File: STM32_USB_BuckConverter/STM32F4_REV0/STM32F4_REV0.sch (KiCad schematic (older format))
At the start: 41 parts

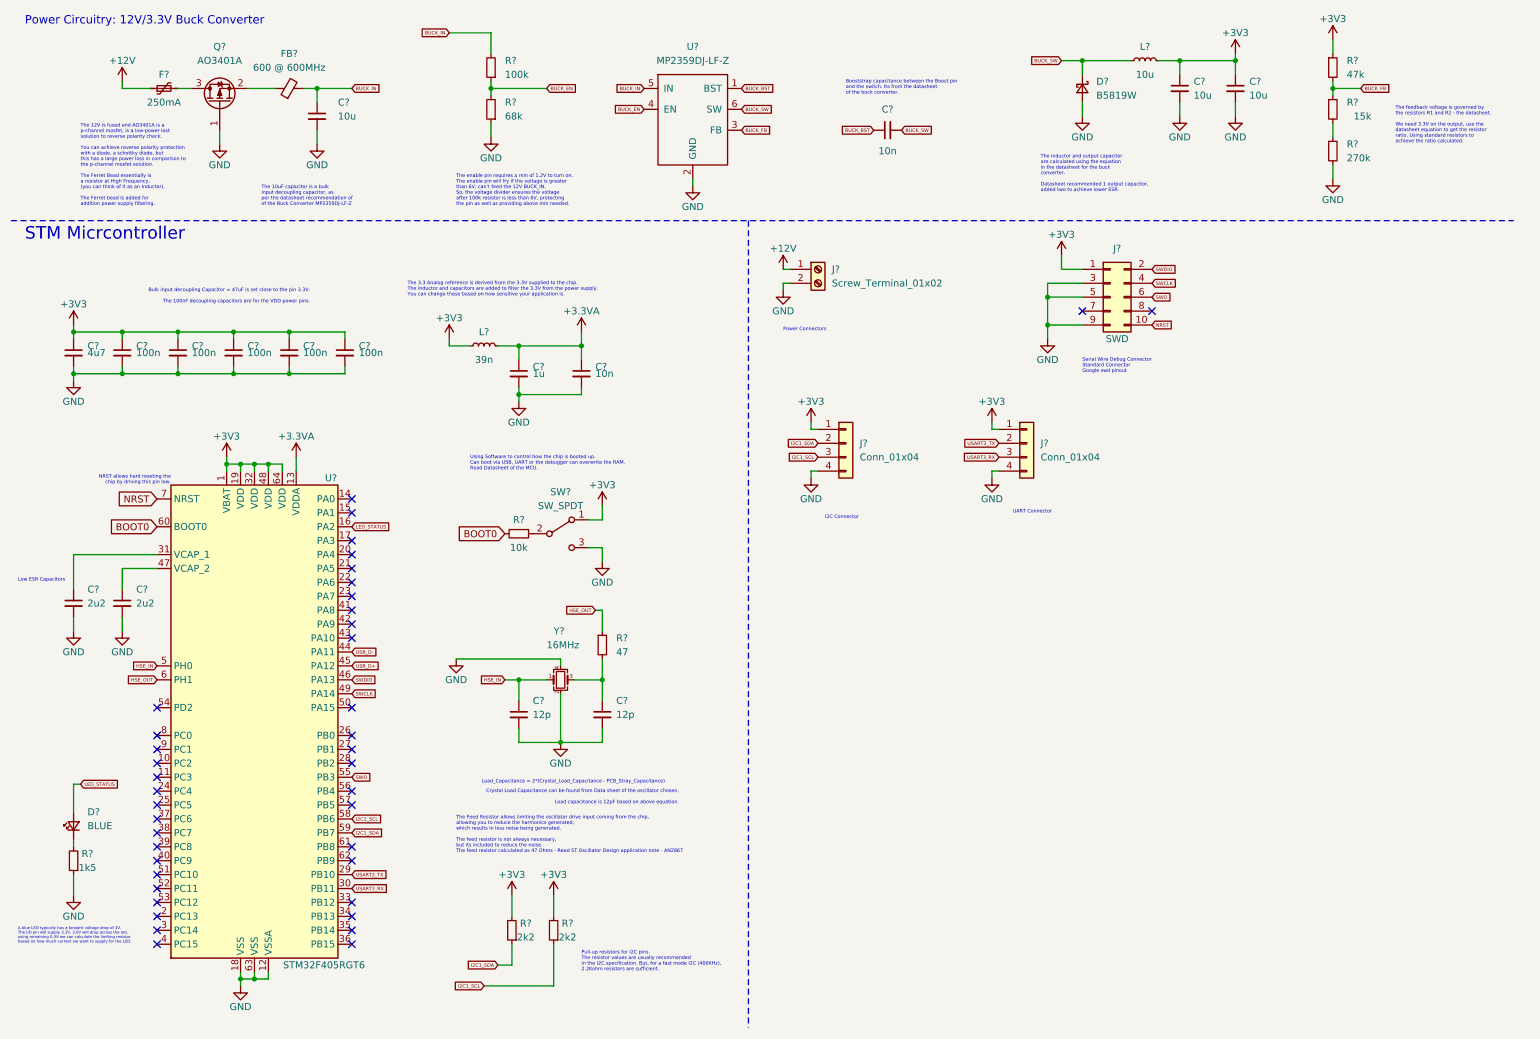
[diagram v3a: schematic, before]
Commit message: Added USB micro connector. Also added schottky diode in the power circuitry incase we want to power the board with USB and not the 12V. The schottky diode will protect incase both 12V present and the USB connected, the 12V will reverse biase the schottky diode.
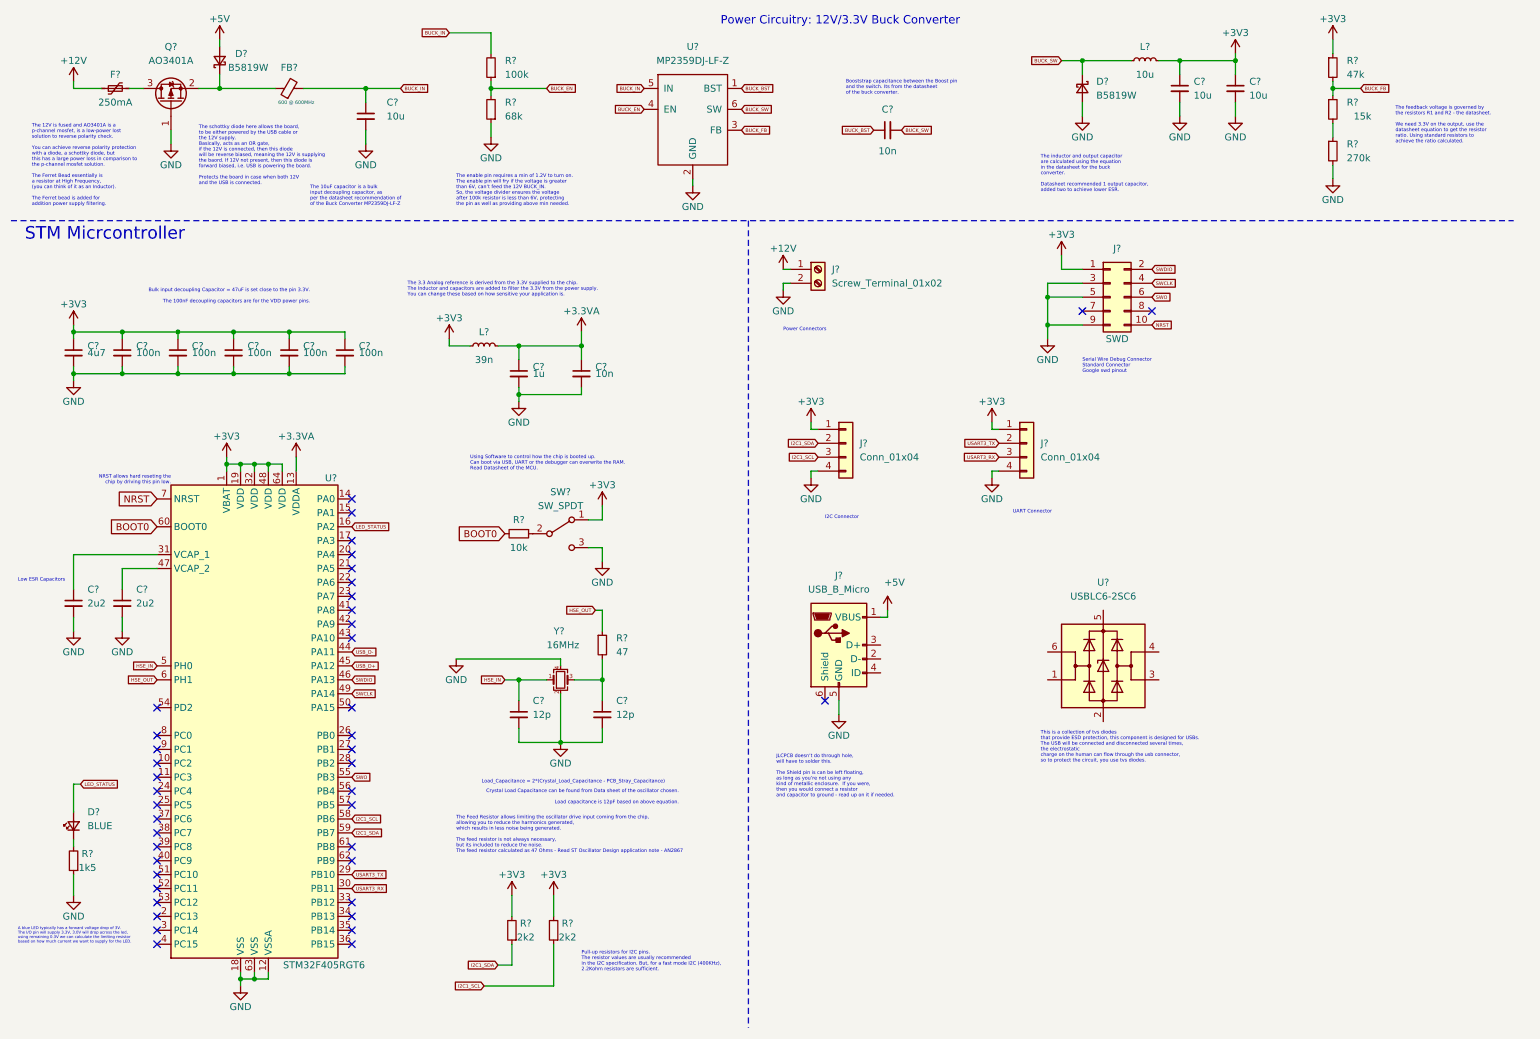
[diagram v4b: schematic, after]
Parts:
- added D?: B5819W, symbol Device:D_Schottky_Small
- added J?: USB_B_Micro, symbol Connector:USB_B_Micro
- added U?: USBLC6-2SC6, Package_TO_SOT_SMD:SOT-23-6, symbol Power_Protection:USBLC6-2SC6
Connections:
- net GND: now also J?.5 (GND)
- net at FB?.1, Q?.2 (S): now also D?.1 (K)
- new net +5V: D?.2 (A), J?.1 (VBUS)
- no-connect marks 41 -> 42
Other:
- note added: "JLCPCB doesn’t do through hole, \nwill have to solder this. \n\nThe Shield pin is can be left floating, \nas long as you’re not using any \nkind of metallic enclosure. If you were, \nthen you would connect a resistor\nand capacitor to ground - read up on it if needed."
- note added: "The schottky diode here allows the board, \nto be either powered by the USB cable or \nthe 12V supply. \nBasically, acts as an OR gate, \nif the 12V is connected, then this diode\nwill be reverse biased, meaning the 12V is supplying\nthe baord. If 12V not present, then this diode is \nforward biased, i.e. USB is powering the board. \n\nProtects the board in case when both 12V \nand the USB is con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"
- note added: "This is a collection of tvs diodes \nthat provide ESD protection, this component is designed for USBs. \nThe USB will be connected and disconnected several times, \nthe electrostatic\ncharge on the human can flow through the usb connector, \nso to protect the circuit, you use tvs diodes. \n"
- moved on the sheet: C?, F?, Q?
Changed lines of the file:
@@
-$EndComp
-$Comp
-L power:+12V #PWR?
-U 1 1 6070A53E
-P 1250 1000
-F 0 "#PWR?" H 1250 850 50  0001 C CNN
-F 1 "+12V" H 1250 1150 50  0000 C CNN
-F 2 "" H 1250 1000 50  0001 C CNN
-F 3 "" H 1250 1000 50  0001 C CNN
-	1    1250 1000
-	1    0    0    -1
-$EndComp
-$Comp
-L Device:Polyfuse_Small F?
-U 1 1 6070BEAF
-P 1550 1050
-F 0 "F?" V 1650 1050 50  0000 C CNN
-F 1 "250mA" V 1450 1050 50  0000 C CNN
-F 2 "" H 1600 850 50  0001 L CNN
-F 3 "~" H 1550 1050 50  0001 C CNN
-	1    1550 1050
-	0    -1   -1   0
-$EndComp
-$Comp
-L power:GND #PWR?
-U 1 1 60714FBD
-P 1950 1450
-F 0 "#PWR?" H 1950 1200 50  0001 C CNN
-F 1 "GND" H 1950 1300 50  0000 C CNN
-F 2 "" H 1950 1450 50  0001 C CNN
-F 3 "" H 1950 1450 50  0001 C CNN
-	1    1950 1450
-	-1   0    0    -1
-$EndComp
-Wire Wire Line
-	1950 1350 1950 1450
-Wire Wire Line
-	1650 1050 1750 1050
-Text Notes 950  1900 0    25   ~ 0
-The 12V is fused and AO3401A is a \np-channel mosfet, is a low-power lost \nsolution to reverse polarity check. \n\nYou can achieve reverse polarity protection \nwith a diode, a schottky diode, but \nthis has a large power loss in comparison to \nthe p-channel mosfet solution. \n\nThe Ferret Bead essentially is \na resistor at High Frequency, \n(you can think of it as an Inductor). \n\nThe Ferret bead is added for \naddition power supply filtering. \n
-Wire Wire Line
-	2350 1050 2150 1050
-$Comp
-L Transistor_FET:AO3401A Q?
-U 1 1 6070E341
-P 1950 1150
-F 0 "Q?" V 2350 1150 50  0000 C CNN
-F 1 "AO3401A" V 2250 1150 50  0000 C CNN
-F 2 "Package_TO_SOT_SMD:SOT-23" H 2150 1075 50  0001 L CIN
-F 3 "http://www.aosmd.com/pdfs/datasheet/AO3401A.pdf" H 1950 1150 50  0001 L CNN
-	1    1950 1150
-	0    -1   -1   0
 $EndComp
 $Comp
@@
 U 1 1 607283EA
 P 2450 1050
-F 0 "FB?" V 2700 1050 50  0000 C CNN
-F 1 "600 @ 600MHz" V 2600 1050 50  0000 C CNN
+F 0 "FB?" V 2600 1050 50  0000 C CNN
+F 1 "600 @ 600MHz" V 2350 1000 25  0000 C CNN
 F 2 "" V 2380 1050 50  0001 C CNN
 F 3 "~" H 2450 1050 50  0001 C CNN
@@
 L Device:C_Small C?
 U 1 1 607304BE
-P 2650 1250
-F 0 "C?" H 2800 1350 50  0000 L CNN
-F 1 "10u" H 2800 1250 50  0000 L CNN
-F 2 "" H 2650 1250 50  0001 C CNN
-F 3 "~" H 2650 1250 50  0001 C CNN
-	1    2650 1250
-	1    0    0    -1
-$EndComp
-Wire Wire Line
-	2550 1050 2650 1050
-Wire Wire Line
-	2650 1050 2650 1150
+P 3000 1250
+F 0 "C?" H 3150 1350 50  0000 L CNN
+F 1 "10u" H 3150 1250 50  0000 L CNN
+F 2 "" H 3000 1250 50  0001 C CNN
+F 3 "~" H 3000 1250 50  0001 C CNN
+	1    3000 1250
+	1    0    0    -1
+$EndComp
+Wire Wire Line
+	3000 1050 3000 1150
 $Comp
 L power:GND #PWR?
 U 1 1 60733C86
-P 2650 1450
-F 0 "#PWR?" H 2650 1200 50  0001 C CNN
-F 1 "GND" H 2650 1300 50  0000 C CNN
-F 2 "" H 2650 1450 50  0001 C CNN
-F 3 "" H 2650 1450 50  0001 C CNN
-	1    2650 1450
-	-1   0    0    -1
-$EndComp
-Wire Wire Line
-	2650 1350 2650 1450
-Text Notes 2250 1900 0    25   ~ 0
+P 3000 1450
+F 0 "#PWR?" H 3000 1200 50  0001 C CNN
+F 1 "GND" H 3000 1300 50  0000 C CNN
+F 2 "" H 3000 1450 50  0001 C CNN
+F 3 "" H 3000 1450 50  0001 C CNN
+	1    3000 1450
+	-1   0    0    -1
+$EndComp
+Wire Wire Line
+	3000 1350 3000 1450
+Text Notes 2600 1900 0    25   ~ 0
 The 10uF capacitor is a bulk \ninput decoupling capacitor, as \nper the datasheet recommendation of \nof the Buck Converter MP2359DJ-LF-Z
-Text GLabel 2900 1050 2    25   Input ~ 0
+Text GLabel 3250 1050 2    25   Input ~ 0
 BUCK_IN
 Wire Wire Line
-	2900 1050 2650 1050
-Connection ~ 2650 1050
+	3250 1050 3000 1050
+Connection ~ 3000 1050
 $Comp
 L Device:R_Small R?
@@
 Wire Notes Line
 	450  2000 11250 2000
-Text Notes 550  600  0    60   ~ 0
+Text Notes 5550 600  0    60   ~ 0
 Power Circuitry: 12V/3.3V Buck Converter
-Wire Wire Line
-	1250 1000 1250 1050
-Wire Wire Line
-	1250 1050 1450 1050
 $Comp
 L Connector:Screw_Terminal_01x02 J?
@@
 Text Notes 7650 4150 0    25   ~ 0
 UART Connector\n\n
+$Comp
+L Connector:USB_B_Micro J?
+U 1 1 608B3BCC
+P 6400 5050
+F 0 "J?" H 6400 5550 50  0000 C CNN
+F 1 "USB_B_Micro" H 6400 5450 50  0000 C CNN
+F 2 "" H 6550 5000 50  0001 C CNN
+F 3 "~" H 6550 5000 50  0001 C CNN
+	1    6400 5050
+	1    0    0    -1
+$EndComp
+$Comp
+L power:GND #PWR?
+U 1 1 608B6CA0
+P 6400 5550
+F 0 "#PWR?" H 6400 5300 50  0001 C CNN
+F 1 "GND" H 6400 5400 50  0000 C CNN
+F 2 "" H 6400 5550 50  0001 C CNN
+F 3 "" H 6400 5550 50  0001 C CNN
+	1    6400 5550
+	-1   0    0    -1
+$EndComp
+Wire Wire Line
+	6400 5550 6400 5450
+NoConn ~ 6300 5450
+Text Notes 5950 6150 0    25   ~ 0
+JLCPCB doesn’t do through hole, \nwill have to solder this. \n\nThe Shield pin is can be left floating, \nas long as you’re not using any \nkind of metallic enclosure.  If you were, \nthen you would connect a resistor\nand capacitor to ground - read up on it if needed.
+$Comp
+L Power_Protection:USBLC6-2SC6 U?
+U 1 1 608C7806
+P 8300 5200
+F 0 "U?" H 8300 5800 50  0000 C CNN
+F 1 "USBLC6-2SC6" H 8300 5700 50  0000 C CNN
+F 2 "Package_TO_SOT_SMD:SOT-23-6" H 8300 4700 50  0001 C CNN
+F 3 "https://www.st.com/resource/en/datasheet/usblc6-2.pdf" H 8500 5550 50  0001 C CNN
+	1    8300 5200
+	1    0    0    -1
+$EndComp
+Text Notes 7850 5900 0    25   ~ 0
+This is a collection of tvs diodes \nthat provide ESD protection, this component is designed for USBs. \nThe USB will be connected and disconnected several times, \nthe electrostatic\ncharge on the human can flow through the usb connector, \nso to protect the circuit, you use tvs diodes. \n
+$Comp
+L power:+5V #PWR?
+U 1 1 608CBD21
+P 6750 4800
+F 0 "#PWR?" H 6750 4650 50  0001 C CNN
+F 1 "+5V" H 6800 5000 50  0000 C CNN
+F 2 "" H 6750 4800 50  0001 C CNN
+F 3 "" H 6750 4800 50  0001 C CNN
+	1    6750 4800
+	1    0    0    -1
+$EndComp
+Wire Wire Line
+	6750 4800 6750 4850
+Wire Wire Line
+	6750 4850 6700 4850
+Wire Wire Line
+	900  1050 1100 1050
+Wire Wire Line
+	900  1000 900  1050
+$Comp
+L Transistor_FET:AO3401A Q?
+U 1 1 6070E341
+P 1600 1150
+F 0 "Q?" V 2000 1150 50  0000 C CNN
+F 1 "AO3401A" V 1900 1150 50  0000 C CNN
+F 2 "Package_TO_SOT_SMD:SOT-23" H 1800 1075 50  0001 L CIN
+F 3 "http://www.aosmd.com/pdfs/datasheet/AO3401A.pdf" H 1600 1150 50  0001 L CNN
+	1    1600 1150
+	0    -1   -1   0
+$EndComp
+Text Notes 600  1900 0    25   ~ 0
+The 12V is fused and AO3401A is a \np-channel mosfet, is a low-power lost \nsolution to reverse polarity check. \n\nYou can achieve reverse polarity protection \nwith a diode, a schottky diode, but \nthis has a large power loss in comparison to \nthe p-channel mosfet solution. \n\nThe Ferret Bead essentially is \na resistor at High Frequency, \n(you can think of it as an Inductor). \n\nThe Ferret bead is added for \naddition power supply filtering. \n
+Wire Wire Line
+	1300 1050 1400 1050
+Wire Wire Line
+	1600 1350 1600 1450
+$Comp
+L power:GND #PWR?
+U 1 1 60714FBD
+P 1600 1450
+F 0 "#PWR?" H 1600 1200 50  0001 C CNN
+F 1 "GND" H 1600 1300 50  0000 C CNN
+F 2 "" H 1600 1450 50  0001 C CNN
+F 3 "" H 1600 1450 50  0001 C CNN
+	1    1600 1450
+	-1   0    0    -1
+$EndComp
+$Comp
+L Device:Polyfuse_Small F?
+U 1 1 6070BEAF
+P 1200 1050
+F 0 "F?" V 1300 1050 50  0000 C CNN
+F 1 "250mA" V 1100 1050 50  0000 C CNN
+F 2 "" H 1250 850 50  0001 L CNN
+F 3 "~" H 1200 1050 50  0001 C CNN
+	1    1200 1050
+	0    -1   -1   0
+$EndComp
+$Comp
+L power:+12V #PWR?
+U 1 1 6070A53E
+P 900 1000
+F 0 "#PWR?" H 900 850 50  0001 C CNN
+F 1 "+12V" H 900 1150 50  0000 C CNN
+F 2 "" H 900 1000 50  0001 C CNN
+F 3 "" H 900 1000 50  0001 C CNN
+	1    900  1000
+	1    0    0    -1
+$EndComp
+$Comp
+L Device:D_Schottky_Small D?
+U 1 1 608E7448
+P 1950 850
+F 0 "D?" V 2000 650 50  0000 L CNN
+F 1 "B5819W" V 1900 500 50  0000 L CNN
+F 2 "" V 1950 850 50  0001 C CNN
+F 3 "~" V 1950 850 50  0001 C CNN
+	1    1950 850
+	0    -1   -1   0
+$EndComp
+Wire Wire Line
+	2550 1050 3000 1050
+Wire Wire Line
+	1950 950  1950 1050
+Wire Wire Line
+	1950 1050 1800 1050
+Wire Wire Line
+	1950 1050 2350 1050
+Connection ~ 1950 1050
+$Comp
+L power:+5V #PWR?
+U 1 1 6090AF68
+P 1950 700
+F 0 "#PWR?" H 1950 550 50  0001 C CNN
+F 1 "+5V" H 1950 850 50  0000 C CNN
+F 2 "" H 1950 700 50  0001 C CNN
+F 3 "" H 1950 700 50  0001 C CNN
+	1    1950 700
+	1    0    0    -1
+$EndComp
+Wire Wire Line
+	1950 700  1950 750
+Text Notes 1800 1750 0    25   ~ 0
+The schottky diode here allows the board, \nto be either powered by the USB cable or \nthe 12V supply. \nBasically, acts as an OR gate, \nif the 12V is connected, then this diode\nwill be reverse biased, meaning the 12V is supplying\nthe baord. If 12V not present, then this diode is \nforward biased, i.e. USB is powering the board. \n\nProtects the board in case when both 12V \nand the USB is connected.
 $EndSCHEMATC

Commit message: Added ESD protection component for the USB connector.
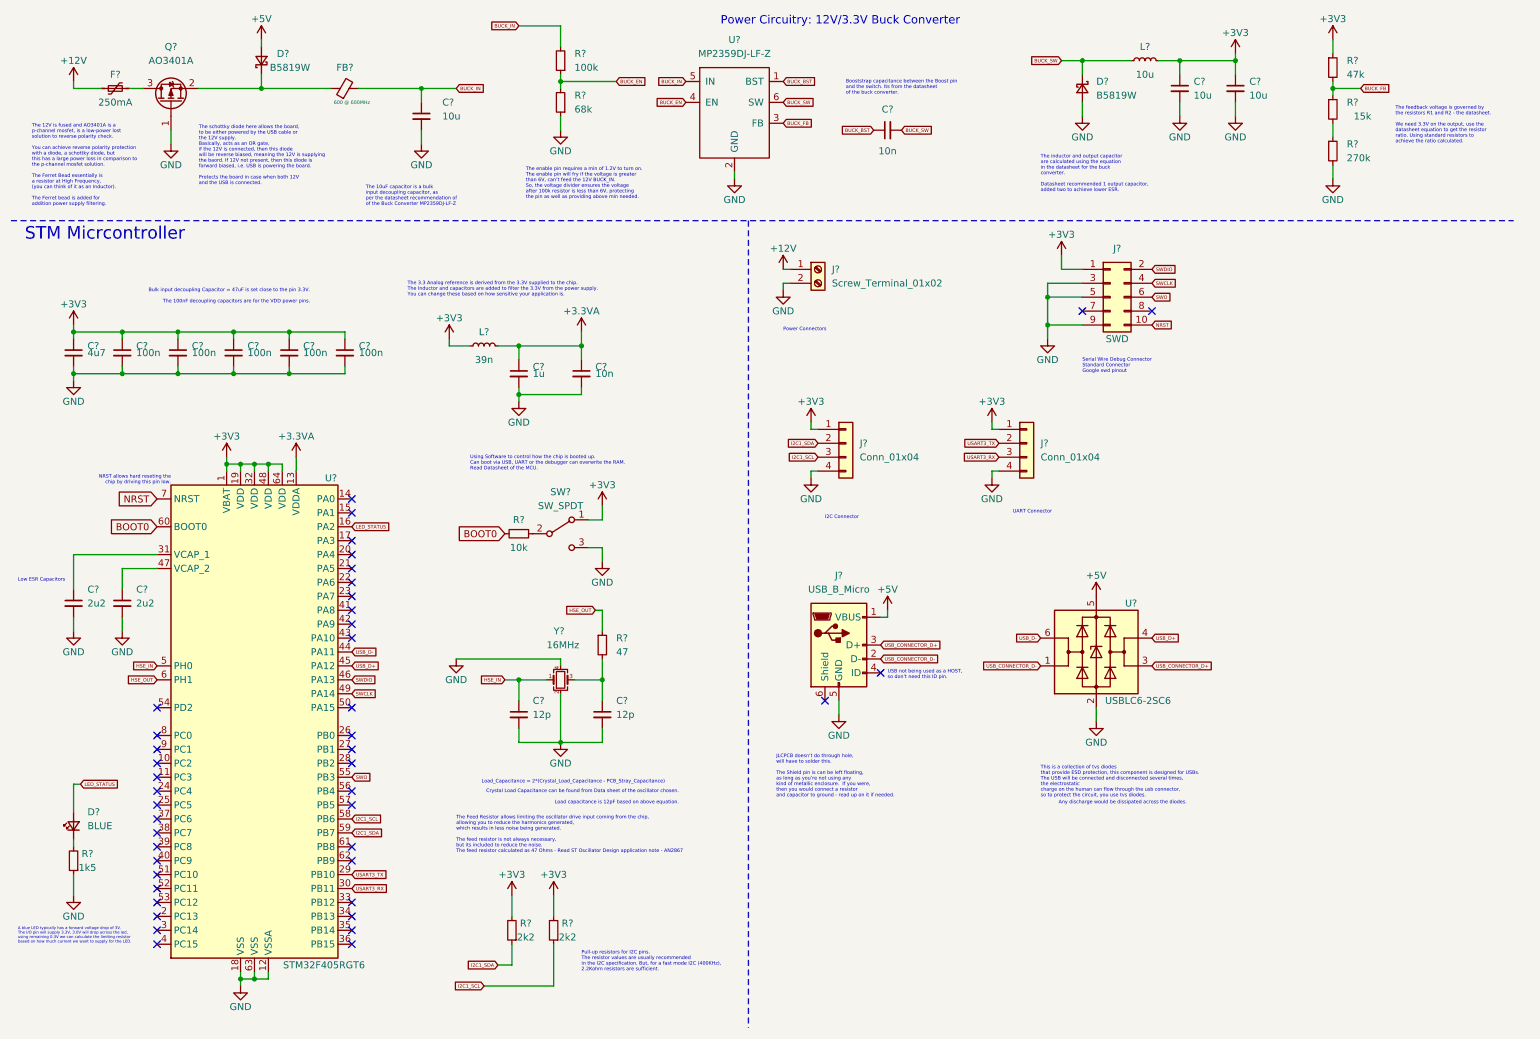
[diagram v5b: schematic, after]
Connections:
- net +5V: now also U?.5 (VBUS)
- net GND: now also U?.2 (GND)
- net USB_D+: now also U?.4 (I/O2)
- net USB_D-: now also U?.6 (I/O1)
- net USB_CONNECTOR_D-: now reaches J?.2 (D-)
- net USB_CONNECTOR_D-: now also U?.1 (I/O1)
- net USB_CONNECTOR_D+: now reaches J?.3 (D+)
- net USB_CONNECTOR_D+: now also U?.3 (I/O2)
- no-connect marks 42 -> 43
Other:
- note added: "Any discharge would be dissipated across the diodes."
- note added: "USB not being used as a HOST, \nso don’t need this ID pin."
- moved on the sheet: C?, D?, FB?, R?, U?
